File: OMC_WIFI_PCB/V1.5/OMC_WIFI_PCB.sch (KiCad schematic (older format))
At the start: 26 parts, among them J1 Conn_01x02_Male, J10 Conn_01x01_Male, J2 Conn_01x02_Female, J3 Conn_01x02_Male, J4 Switch, J5 Pins_FT232R, J6 Level shifter, J7 Conn_01x01_Female, J8 Regulador, J9 Conn_01x01_Female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

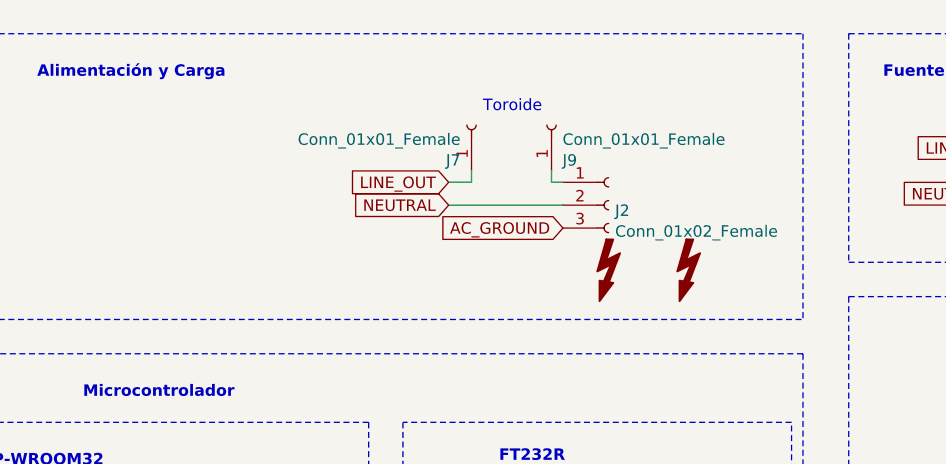
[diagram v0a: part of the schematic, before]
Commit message: Actualización PCB
> Cambio en polaridad de transistor
> Cambio en planos de tierra y B.Mask
> Cambio en librería de conector hembra AC
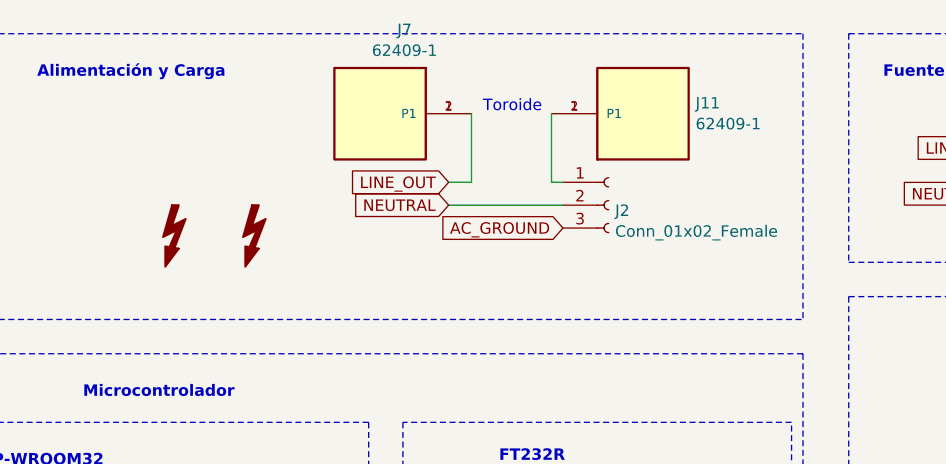
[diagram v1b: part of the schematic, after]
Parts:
- removed J7, J9: Conn_01x01_Female, Connector_Pin:Pin_D1.3mm_L10.0mm_W3.5mm_Flat, symbol Connector:Conn_01x01_Female
- added J11, J7: 62409-1, conector_espada:espada, symbol espada:62409-1
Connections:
- net LINE_OUT: now also J7.1 (P1), J7.2 (P1)
- net at J2.1 (Pin_1): now also J11.1 (P1), J11.2 (P1)
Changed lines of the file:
@@
 L Graphic:SYM_Flash_Small SYM1
 U 1 1 6268094E
-P 5350 1650
-F 0 "SYM1" V 5260 1650 50  0001 C CNN
-F 1 "SYM_Flash_Small" V 5440 1650 50  0001 C CNN
-F 2 "Symbol:Symbol_HighVoltage_Type2_CopperTop_VerySmall" H 5350 1874 50  0001 C CNN
-F 3 "~" H 5750 1550 50  0001 C CNN
-	1    5350 1650
+P 3450 1500
+F 0 "SYM1" V 3360 1500 50  0001 C CNN
+F 1 "SYM_Flash_Small" V 3540 1500 50  0001 C CNN
+F 2 "Symbol:Symbol_HighVoltage_Type2_CopperTop_VerySmall" H 3450 1724 50  0001 C CNN
+F 3 "~" H 3850 1400 50  0001 C CNN
+	1    3450 1500
 	1    0    0    -1
 $EndComp
@@
 L Graphic:SYM_Flash_Small SYM2
 U 1 1 6268B7DC
-P 5700 1650
-F 0 "SYM2" V 5610 1650 50  0001 C CNN
-F 1 "SYM_Flash_Small" V 5790 1650 50  0001 C CNN
-F 2 "Symbol:Symbol_HighVoltage_Type2_CopperTop_VerySmall" H 5700 1874 50  0001 C CNN
-F 3 "~" H 6100 1550 50  0001 C CNN
-	1    5700 1650
+P 3800 1500
+F 0 "SYM2" V 3710 1500 50  0001 C CNN
+F 1 "SYM_Flash_Small" V 3890 1500 50  0001 C CNN
+F 2 "Symbol:Symbol_HighVoltage_Type2_CopperTop_VerySmall" H 3800 1724 50  0001 C CNN
+F 3 "~" H 4200 1400 50  0001 C CNN
+	1    3800 1500
 	1    0    0    -1
 $EndComp
@@
 Text Notes 6970 2140 0    50   ~ 10
 Relay\n
-$Comp
-L Connector:Conn_01x01_Female J7
-U 1 1 6284CB5E
-P 4750 1000
-F 0 "J7" V 4596 1048 50  0000 L CNN
-F 1 "Conn_01x01_Female" V 4687 1048 50  0000 L CNN
-F 2 "Connector_Pin:Pin_D1.3mm_L10.0mm_W3.5mm_Flat" H 4750 1000 50  0001 C CNN
-F 3 "~" H 4750 1000 50  0001 C CNN
-	1    4750 1000
-	0    -1   -1   0
-$EndComp
-$Comp
-L Connector:Conn_01x01_Female J9
-U 1 1 62853AFC
-P 5100 1000
-F 0 "J9" V 4946 1048 50  0000 L CNN
-F 1 "Conn_01x01_Female" V 5037 1048 50  0000 L CNN
-F 2 "Connector_Pin:Pin_D1.3mm_L10.0mm_W3.5mm_Flat" H 5100 1000 50  0001 C CNN
-F 3 "~" H 5100 1000 50  0001 C CNN
-	1    5100 1000
-	0    1    -1   0
-$EndComp
 Wire Notes Line
 	750  600  6200 600
@@
 	750  1850 6200 1850
 Wire Wire Line
-	5100 1200 5100 1250
-Wire Wire Line
 	4650 1250 4750 1250
-Wire Wire Line
-	4750 1250 4750 1200
 Wire Wire Line
 	5100 1250 5150 1250
@@
 Text GLabel 5150 1450 0    50   Input ~ 0
 AC_GROUND
+$Comp
+L espada:62409-1 J11
+U 1 1 628EB61B
+P 5500 950
+F 0 "J11" H 5730 996 50  0000 L CNN
+F 1 "62409-1" H 5730 905 50  0000 L CNN
+F 2 "conector_espada:espada" H 5500 950 50  0001 L BNN
+F 3 "" H 5500 950 50  0001 L BNN
+F 4 "62409-1" H 5500 950 50  0001 L BNN "Comment"
+F 5 "Compliant" H 5500 950 50  0001 L BNN "EU_RoHS_Compliance"
+	1    5500 950
+	1    0    0    -1
+$EndComp
+Wire Wire Line
+	5100 950  5100 1250
+Wire Wire Line
+	4750 950  4750 1250
+$Comp
+L espada:62409-1 J7
+U 1 1 62907647
+P 4350 950
+F 0 "J7" H 4243 583 50  0000 C CNN
+F 1 "62409-1" H 4243 674 50  0000 C CNN
+F 2 "conector_espada:espada" H 4350 950 50  0001 L BNN
+F 3 "" H 4350 950 50  0001 L BNN
+F 4 "62409-1" H 4350 950 50  0001 L BNN "Comment"
+F 5 "Compliant" H 4350 950 50  0001 L BNN "EU_RoHS_Compliance"
+	1    4350 950
+	-1   0    0    1
+$EndComp
 $EndSCHEMATC

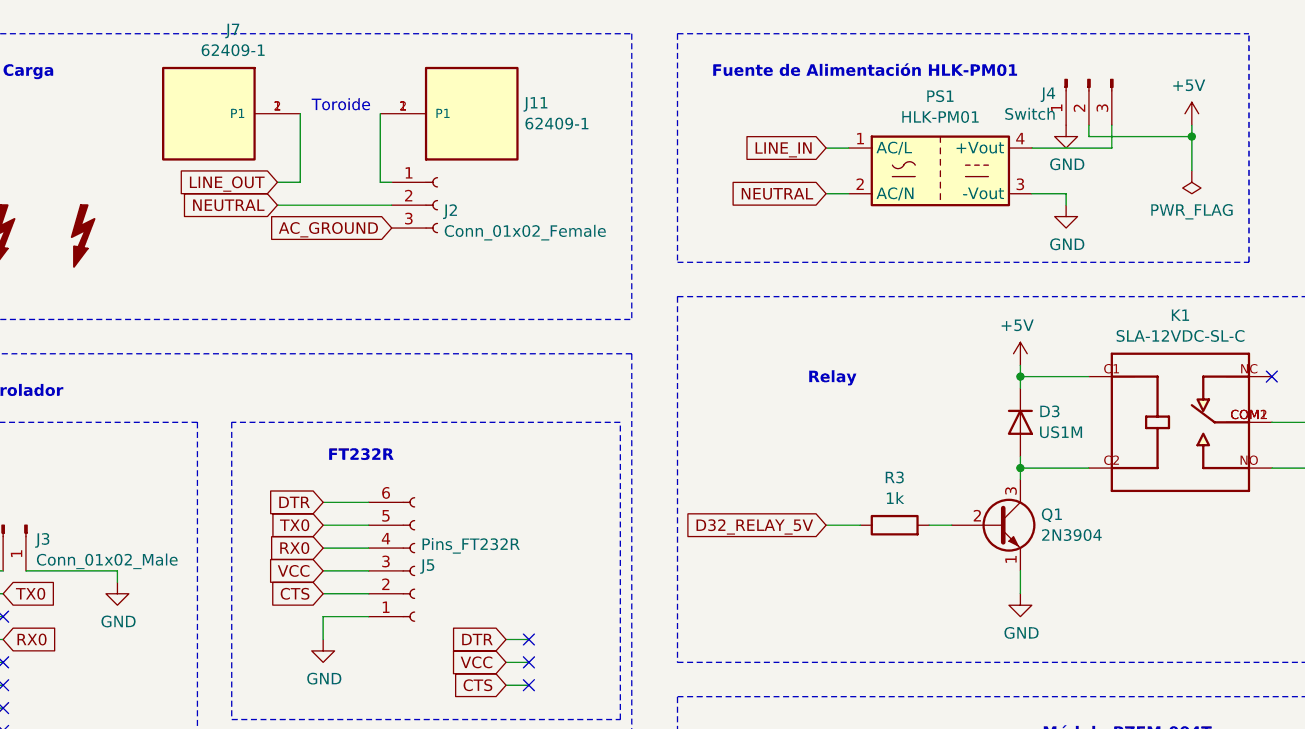
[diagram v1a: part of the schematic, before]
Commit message: Creación de GERBERS PCB v1.5
Se incluyen cambios pequeños en la PCB:
> Cambio al transistor MMBT3904
> Cambio en puntos de soldadura para los cables del toroide.
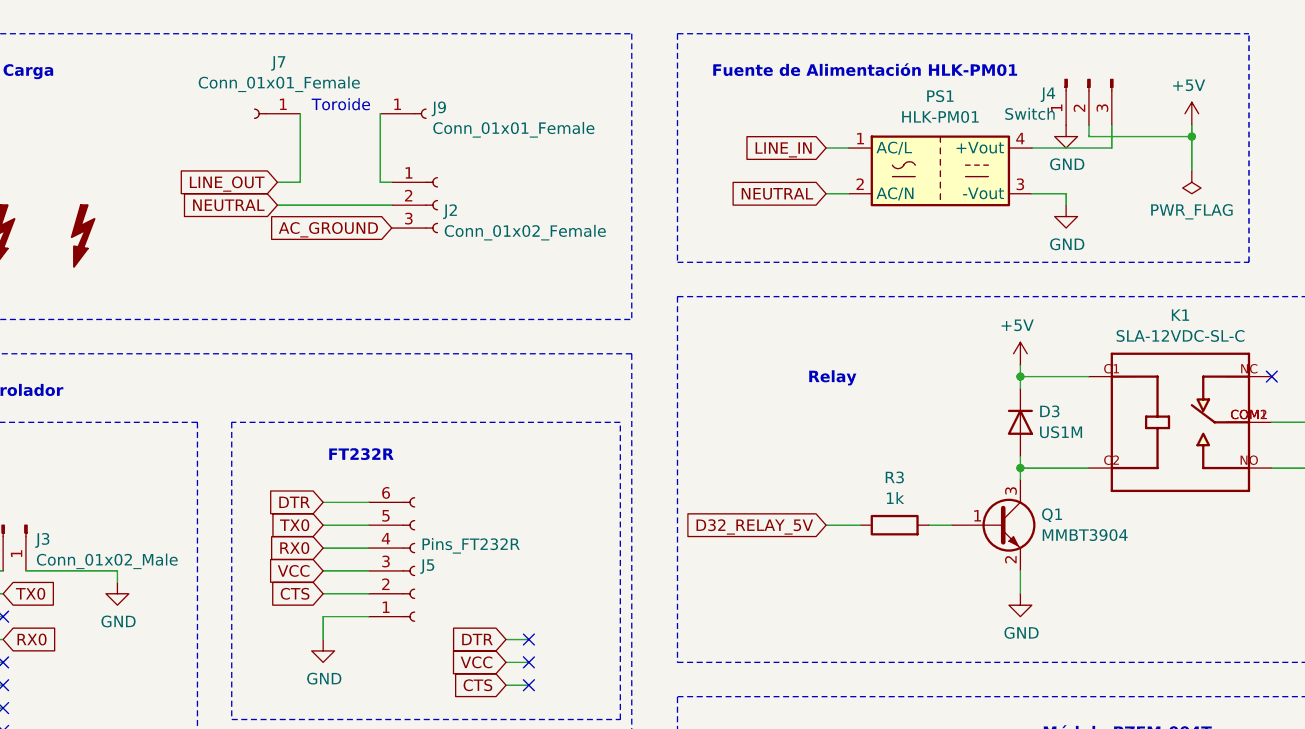
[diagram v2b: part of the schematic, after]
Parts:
- removed J11, J7: 62409-1, conector_espada:espada, symbol espada:62409-1
- removed Q1: 2N3904, Package_TO_SOT_SMD:SC-59_Handsoldering, symbol Transistor_BJT:2N3904
- added J7, J9: Conn_01x01_Female, Connector_Wire:SolderWire-1.5sqmm_1x01_D1.7mm_OD3mm, symbol Connector:Conn_01x01_Female
- added Q1: MMBT3904, Package_TO_SOT_SMD:SOT-23, symbol Transistor_BJT:MMBT3904
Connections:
- net GND: now also Q1.2 (E)
- net LINE_OUT: now also J7.1 (Pin_1)
- net at R3.2: now also Q1.1 (B)
- net at D3.2 (A), K1.C2: now also Q1.3 (C)
- net at J2.1 (Pin_1): now also J9.1 (Pin_1)
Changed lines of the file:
@@
-$EndComp
-$Comp
-L Transistor_BJT:2N3904 Q1
-U 1 1 6251C78E
-P 7800 2750
-F 0 "Q1" H 7990 2796 50  0000 L CNN
-F 1 "2N3904" H 7990 2705 50  0000 L CNN
-F 2 "Package_TO_SOT_SMD:SC-59_Handsoldering" H 8000 2675 50  0001 L CIN
-F 3 "https://www.onsemi.com/pub/Collateral/2N3903-D.PDF" H 7800 2750 50  0001 L CNN
-	1    7800 2750
-	1    0    0    -1
 $EndComp
 $Comp
@@
 Text GLabel 5150 1450 0    50   Input ~ 0
 AC_GROUND
-$Comp
-L espada:62409-1 J11
-U 1 1 628EB61B
-P 5500 950
-F 0 "J11" H 5730 996 50  0000 L CNN
-F 1 "62409-1" H 5730 905 50  0000 L CNN
-F 2 "conector_espada:espada" H 5500 950 50  0001 L BNN
-F 3 "" H 5500 950 50  0001 L BNN
-F 4 "62409-1" H 5500 950 50  0001 L BNN "Comment"
-F 5 "Compliant" H 5500 950 50  0001 L BNN "EU_RoHS_Compliance"
-	1    5500 950
-	1    0    0    -1
-$EndComp
 Wire Wire Line
 	5100 950  5100 1250
@@
 	4750 950  4750 1250
 $Comp
-L espada:62409-1 J7
-U 1 1 62907647
-P 4350 950
-F 0 "J7" H 4243 583 50  0000 C CNN
-F 1 "62409-1" H 4243 674 50  0000 C CNN
-F 2 "conector_espada:espada" H 4350 950 50  0001 L BNN
-F 3 "" H 4350 950 50  0001 L BNN
-F 4 "62409-1" H 4350 950 50  0001 L BNN "Comment"
-F 5 "Compliant" H 4350 950 50  0001 L BNN "EU_RoHS_Compliance"
-	1    4350 950
+L Connector:Conn_01x01_Female J9
+U 1 1 629675E0
+P 5300 950
+F 0 "J9" H 5328 976 50  0000 L CNN
+F 1 "Conn_01x01_Female" H 5328 885 50  0000 L CNN
+F 2 "Connector_Wire:SolderWire-1.5sqmm_1x01_D1.7mm_OD3mm" H 5300 950 50  0001 C CNN
+F 3 "~" H 5300 950 50  0001 C CNN
+	1    5300 950
+	1    0    0    -1
+$EndComp
+$Comp
+L Connector:Conn_01x01_Female J7
+U 1 1 6296884C
+P 4550 950
+F 0 "J7" H 4442 725 50  0000 C CNN
+F 1 "Conn_01x01_Female" H 4442 816 50  0000 C CNN
+F 2 "Connector_Wire:SolderWire-1.5sqmm_1x01_D1.7mm_OD3mm" H 4550 950 50  0001 C CNN
+F 3 "~" H 4550 950 50  0001 C CNN
+	1    4550 950
 	-1   0    0    1
 $EndComp
+$Comp
+L Transistor_BJT:MMBT3904 Q1
+U 1 1 6298E1FD
+P 7800 2750
+F 0 "Q1" H 7991 2796 50  0000 L CNN
+F 1 "MMBT3904" H 7991 2705 50  0000 L CNN
+F 2 "Package_TO_SOT_SMD:SOT-23" H 8000 2675 50  0001 L CIN
+F 3 "https://www.onsemi.com/pub/Collateral/2N3903-D.PDF" H 7800 2750 50  0001 L CNN
+	1    7800 2750
+	1    0    0    -1
+$EndComp
 $EndSCHEMATC
